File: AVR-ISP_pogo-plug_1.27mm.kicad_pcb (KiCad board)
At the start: 2 copper layers, 10 x 19.2 mm, 4 parts, among them P1 CONN_6, P2 CONN_6

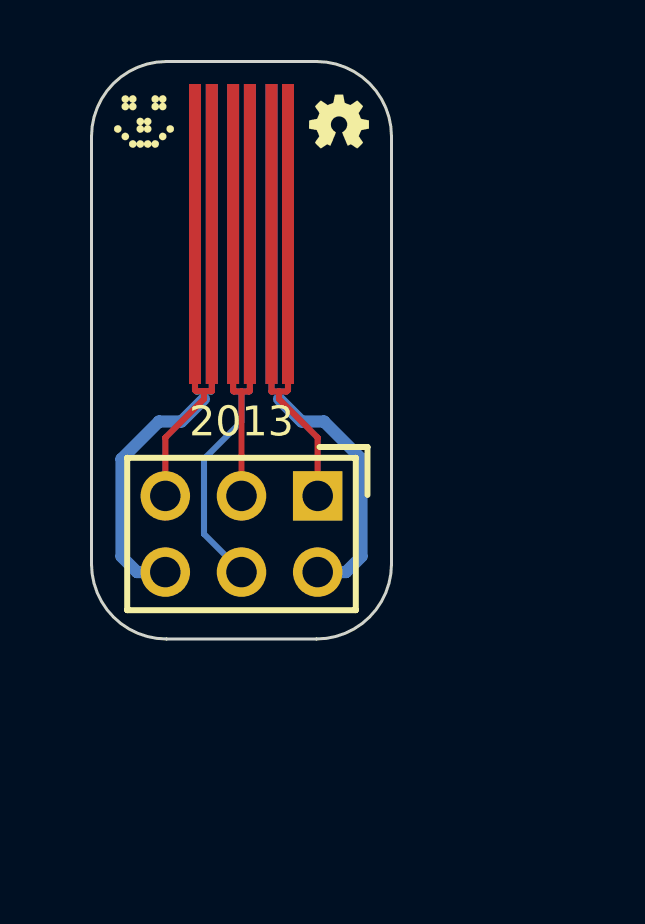
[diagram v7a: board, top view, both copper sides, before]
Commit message: Changed the board-outline a bit.
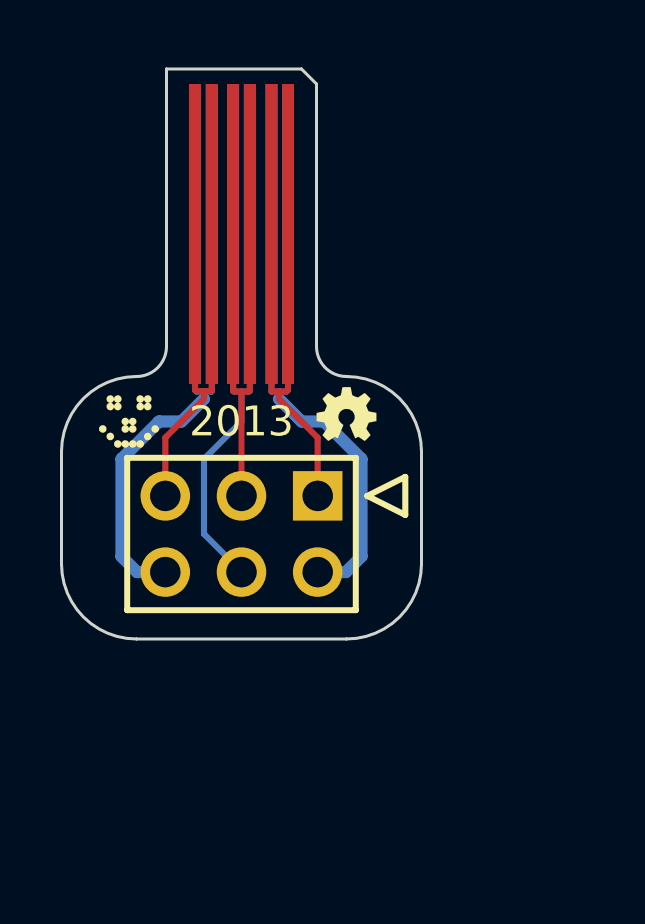
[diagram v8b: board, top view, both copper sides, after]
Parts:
- moved G1 10.0 mm to (64.8, 74.2)
- moved G2 9.75 mm to (72.0, 74.0)
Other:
- board size 10 x 19.2 mm -> 12 x 19 mm
- board text added: "goo.gl/rwxuRB"
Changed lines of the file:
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@@
     (links 12)
     (no_connects 0)
-    (area 63.449999 62.199999 73.550001 82.6228)
+    (area 62.449999 62.449999 74.550001 81.550001)
     (thickness 1.6)
-    (drawings 9)
+    (drawings 15)
     (tracks 59)
     (zones 0)
@@
     (0 B.Cu signal)
     (20 B.SilkS user)
-    (21 F.SilkS user hide)
+    (21 F.SilkS user)
     (22 B.Mask user)
     (23 F.Mask user)
@@
     (pad_drill 0)
     (pad_to_mask_clearance 0)
+    (solder_mask_min_width 0.3)
     (aux_axis_origin 0 0)
     (visible_elements FFFFF77F)
@@
       (net 1 /GND))
   )
+  (module pin_array_3x2 (layer F.Cu)
+    (at 68.5 78 180)
+    (descr "Double rangee de contacts 2 x 4 pins")
+    (tags CONN)
+    (fp_text reference P1 (at 0 -2.5 180) (layer F.SilkS) hide
+      (effects (font (size 1.016 1.016) (thickness 0.2032)))
+    )
+    (fp_text value CONN_6 (at 0 3.81 180) (layer F.SilkS) hide
+      (effects (font (size 1.016 1.016) (thickness 0.2032)))
+    )
+    (fp_line (start -4.191 1.27) (end -5.461 0.635) (layer F.SilkS) (width 0.2))
+    (fp_line (start -5.461 0.635) (end -5.461 1.905) (layer F.SilkS) (width 0.2))
+    (fp_line (start -5.461 1.905) (end -4.191 1.27) (layer F.SilkS) (width 0.2))
+    (fp_line (start 3.81 2.54) (end -3.81 2.54) (layer F.SilkS) (width 0.2))
+    (fp_line (start -3.81 -2.54) (end 3.81 -2.54) (layer F.SilkS) (width 0.2))
+    (fp_line (start 3.81 -2.54) (end 3.81 2.54) (layer F.SilkS) (width 0.2))
+    (fp_line (start -3.81 2.54) (end -3.81 -2.54) (layer F.SilkS) (width 0.2))
+    (pad 1 thru_hole rect (at -2.54 1.27 180) (size 1.65 1.65) (drill 1.016) (layers *.Cu *.Mask F.SilkS)
+      (net 2 /MISO))
+    (pad 2 thru_hole circle (at -2.54 -1.27 180) (size 1.65 1.65) (drill 1.016) (layers *.Cu *.Mask F.SilkS)
+      (net 6 /V-target))
+    (pad 3 thru_hole circle (at 0 1.27 180) (size 1.65 1.65) (drill 1.016) (layers *.Cu *.Mask F.SilkS)
+      (net 5 /SCK))
+    (pad 4 thru_hole circle (at 0 -1.27 180) (size 1.65 1.65) (drill 1.016) (layers *.Cu *.Mask F.SilkS)
+      (net 3 /MOSI))
+    (pad 5 thru_hole circle (at 2.54 1.27 180) (size 1.65 1.65) (drill 1.016) (layers *.Cu *.Mask F.SilkS)
+      (net 4 /RESET))
+    (pad 6 thru_hole circle (at 2.54 -1.27 180) (size 1.65 1.65) (drill 1.016) (layers *.Cu *.Mask F.SilkS)
+      (net 1 /GND))
+    (model pin_array/pins_array_3x2.wrl
+      (at (xyz 0 0 0))
+      (scale (xyz 1 1 1))
+      (rotate (xyz 0 0 0))
+    )
+  )
   (module OSHW-logo_silkscreen_2mm (layer F.Cu)
-    (at 71.75 64.25)
+    (at 72 74)
     (fp_text reference G2 (at 0 1.05918) (layer F.SilkS) hide
       (effects (font (size 0.127 0.127) (thickness 0.01778)))
@@
   )
   (module LED_smile_silkscreen_2mm (layer F.Cu)
-    (at 65.25 64.25)
+    (at 64.75 74.25)
     (fp_text reference G1 (at 0 1.15062) (layer F.SilkS) hide
       (effects (font (size 0.127 0.127) (thickness 0.00508)))
@@
       (xy 0.32766 -0.38354) (xy 0.35306 -0.37592) (xy 0.3556 -0.37592) (xy 0.381 -0.37338)) (layer F.SilkS) (width 0.00254))
   )
-  (module pin_array_3x2 (layer F.Cu)
-    (at 68.5 78 180)
-    (descr "Double rangee de contacts 2 x 4 pins")
-    (tags CONN)
-    (fp_text reference P1 (at 0 -3.81 180) (layer F.SilkS) hide
-      (effects (font (size 1.016 1.016) (thickness 0.2032)))
-    )
-    (fp_text value CONN_6 (at 0 3.81 180) (layer F.SilkS) hide
-      (effects (font (size 1.016 1.016) (thickness 0.2032)))
-    )
-    (fp_line (start -4.2 2.9) (end -2.6 2.9) (layer F.SilkS) (width 0.2))
-    (fp_line (start -4.2 2.9) (end -4.2 1.3) (layer F.SilkS) (width 0.2))
-    (fp_line (start 3.81 2.54) (end -3.81 2.54) (layer F.SilkS) (width 0.2))
-    (fp_line (start -3.81 -2.54) (end 3.81 -2.54) (layer F.SilkS) (width 0.2))
-    (fp_line (start 3.81 -2.54) (end 3.81 2.54) (layer F.SilkS) (width 0.2))
-    (fp_line (start -3.81 2.54) (end -3.81 -2.54) (layer F.SilkS) (width 0.2))
-    (pad 1 thru_hole rect (at -2.54 1.27 180) (size 1.65 1.65) (drill 1.016) (layers *.Cu *.Mask F.SilkS)
-      (net 2 /MISO))
-    (pad 2 thru_hole circle (at -2.54 -1.27 180) (size 1.65 1.65) (drill 1.016) (layers *.Cu *.Mask F.SilkS)
-      (net 6 /V-target))
-    (pad 3 thru_hole circle (at 0 1.27 180) (size 1.65 1.65) (drill 1.016) (layers *.Cu *.Mask F.SilkS)
-      (net 5 /SCK))
-    (pad 4 thru_hole circle (at 0 -1.27 180) (size 1.65 1.65) (drill 1.016) (layers *.Cu *.Mask F.SilkS)
-      (net 3 /MOSI))
-    (pad 5 thru_hole circle (at 2.54 1.27 180) (size 1.65 1.65) (drill 1.016) (layers *.Cu *.Mask F.SilkS)
-      (net 4 /RESET))
-    (pad 6 thru_hole circle (at 2.54 -1.27 180) (size 1.65 1.65) (drill 1.016) (layers *.Cu *.Mask F.SilkS)
-      (net 1 /GND))
-    (model pin_array/pins_array_3x2.wrl
-      (at (xyz 0 0 0))
-      (scale (xyz 1 1 1))
-      (rotate (xyz 0 0 0))
-    )
-  )
-  (gr_line (start 63.5 79) (end 63.5 64.75) (angle 90) (layer Edge.Cuts) (width 0.1))
-  (gr_line (start 73.5 64.75) (end 73.5 79) (angle 90) (layer Edge.Cuts) (width 0.1))
-  (gr_line (start 66 62.25) (end 71 62.25) (angle 90) (layer Edge.Cuts) (width 0.1))
-  (gr_arc (start 66 64.75) (end 63.5 64.75) (angle 90) (layer Edge.Cuts) (width 0.1))
-  (gr_arc (start 71 64.75) (end 71 62.25) (angle 90) (layer Edge.Cuts) (width 0.1))
-  (gr_line (start 66 81.5) (end 71 81.5) (angle 90) (layer Edge.Cuts) (width 0.1))
-  (gr_arc (start 66 79) (end 66 81.5) (angle 90) (layer Edge.Cuts) (width 0.1))
-  (gr_arc (start 71 79) (end 73.5 79) (angle 90) (layer Edge.Cuts) (width 0.1))
+  (gr_text goo.gl/rwxuRB (at 68.55 74.2) (layer B.SilkS)
+    (effects (font (size 1 0.9) (thickness 0.2)) (justify mirror))
+  )
+  (gr_line (start 71 71.75) (end 71 63) (angle 90) (layer Edge.Cuts) (width 0.1))
+  (gr_line (start 66 62.5) (end 70.5 62.5) (angle 90) (layer Edge.Cuts) (width 0.1))
+  (gr_line (start 70.5 62.5) (end 71 63) (angle 90) (layer Edge.Cuts) (width 0.1))
+  (gr_line (start 66 71.75) (end 66 62.5) (angle 90) (layer Edge.Cuts) (width 0.1))
+  (gr_line (start 65 81.5) (end 72 81.5) (angle 90) (layer Edge.Cuts) (width 0.1))
+  (gr_arc (start 65 71.75) (end 66 71.75) (angle 90) (layer Edge.Cuts) (width 0.1))
+  (gr_arc (start 72 71.75) (end 72 72.75) (angle 90) (layer Edge.Cuts) (width 0.1))
+  (gr_line (start 74.5 79) (end 74.5 75.25) (angle 90) (layer Edge.Cuts) (width 0.1))
+  (gr_line (start 62.5 75.25) (end 62.5 79) (angle 90) (layer Edge.Cuts) (width 0.1))
+  (gr_arc (start 65 75.25) (end 62.5 75.25) (angle 90) (layer Edge.Cuts) (width 0.1))
+  (gr_arc (start 72 75.25) (end 72 72.75) (angle 90) (layer Edge.Cuts) (width 0.1))
+  (gr_arc (start 65 79) (end 65 81.5) (angle 90) (layer Edge.Cuts) (width 0.1))
+  (gr_arc (start 72 79) (end 74.5 79) (angle 90) (layer Edge.Cuts) (width 0.1))
   (gr_text 2013 (at 68.5 74.25) (layer F.SilkS)
     (effects (font (size 1 1) (thickness 0.25)))
